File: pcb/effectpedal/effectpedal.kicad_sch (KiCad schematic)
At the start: 0 parts

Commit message: Made progress on the PCB
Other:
- company: (none) -> Anton Liakhovitch

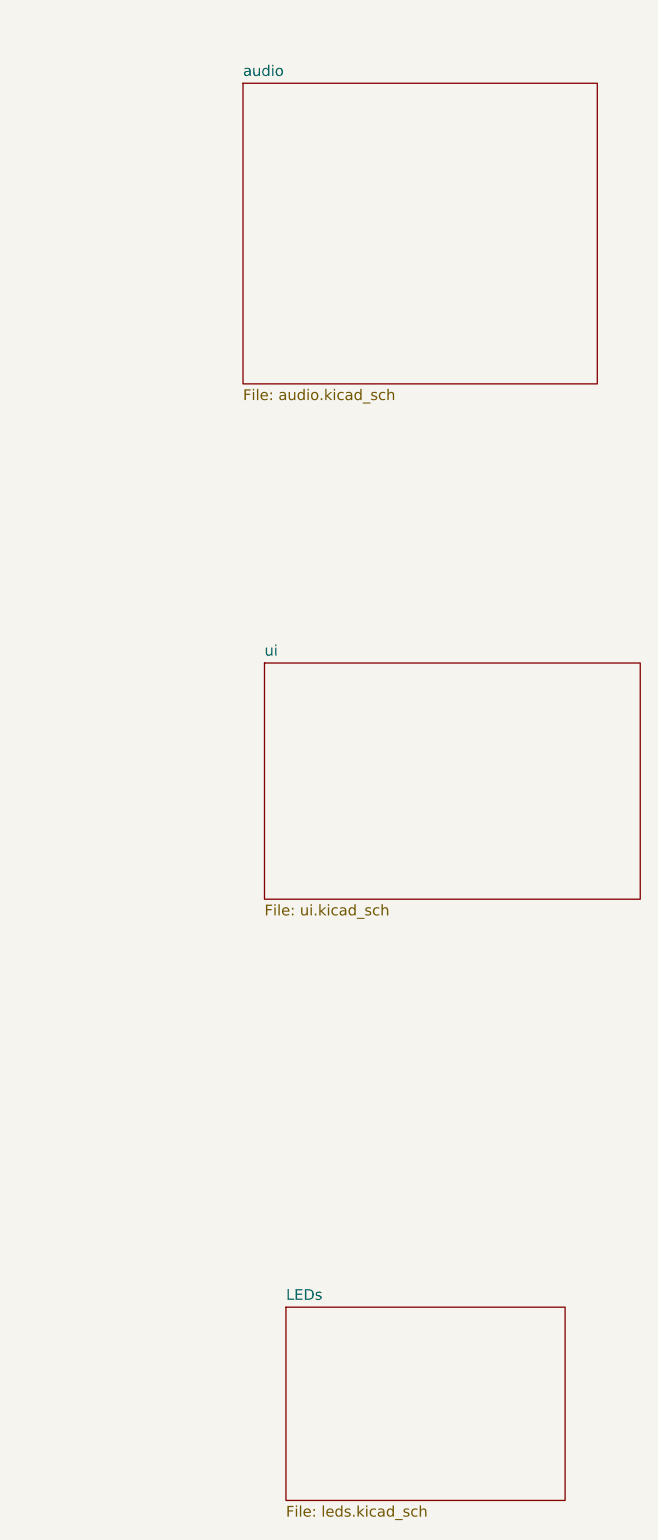
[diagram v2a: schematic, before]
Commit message: Added more test code and deleted some useless stuff
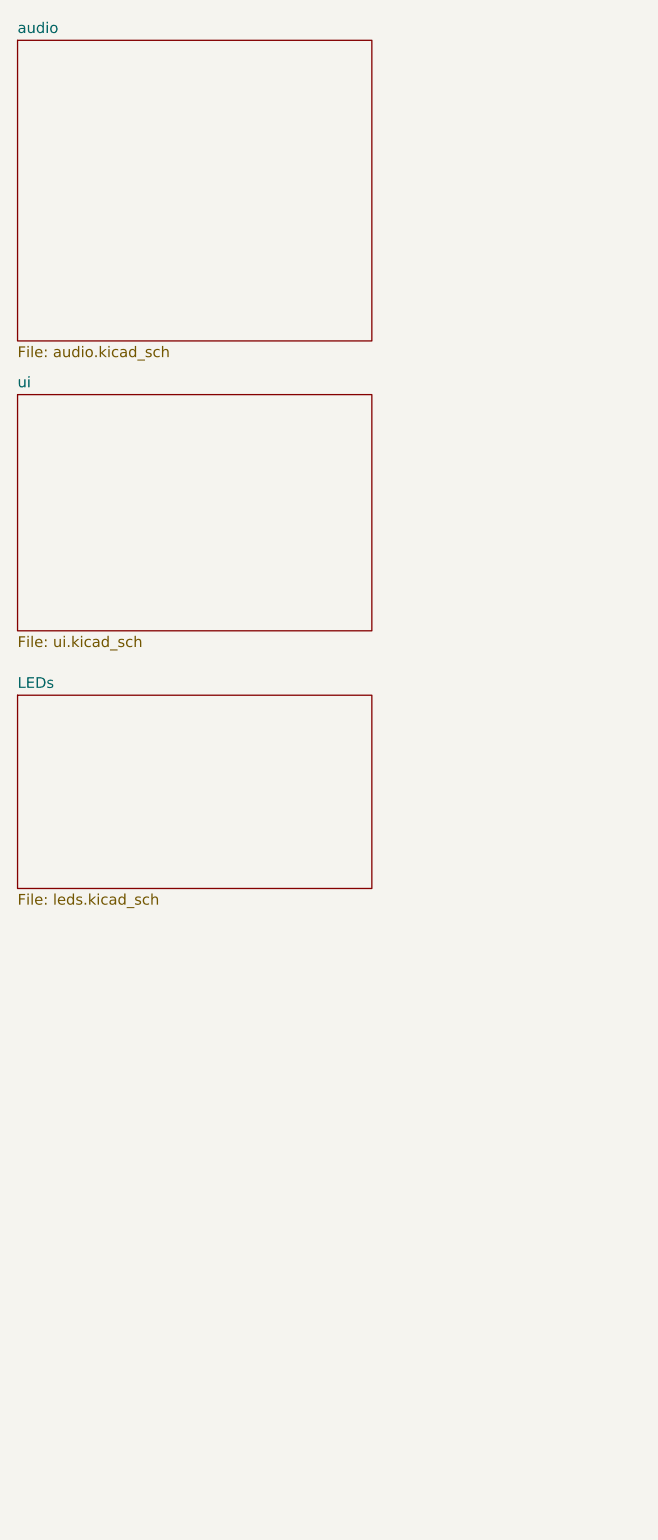
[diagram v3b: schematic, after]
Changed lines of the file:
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@@
     (company "Anton Liakhovitch")
   )
-  (sheet (at 43.18 90.17) (size 44.45 27.94) (fields_autoplaced)
+  (sheet (at 13.97 58.42) (size 41.91 27.94) (fields_autoplaced)
     (stroke (width 0.1524) (type solid) (color 0 0 0 0))
     (fill (color 0 0 0 0.0000))
-    (property "Sheet name" "ui" (id 0) (at 43.18 89.4584 0)
+    (property "Sheet name" "ui" (id 0) (at 13.97 57.7084 0)
       (effects (font (size 1.27 1.27)) (justify left bottom))
     )
-    (property "Sheet file" "ui.kicad_sch" (id 1) (at 43.18 118.6946 0)
+    (property "Sheet file" "ui.kicad_sch" (id 1) (at 13.97 86.9446 0)
       (effects (font (size 1.27 1.27)) (justify left top))
     )
   )
-  (sheet (at 40.64 21.59) (size 41.91 35.56) (fields_autoplaced)
+  (sheet (at 13.97 16.51) (size 41.91 35.56) (fields_autoplaced)
     (stroke (width 0.1524) (type solid) (color 0 0 0 0))
     (fill (color 0 0 0 0.0000))
-    (property "Sheet name" "audio" (id 0) (at 40.64 20.8784 0)
+    (property "Sheet name" "audio" (id 0) (at 13.97 15.7984 0)
       (effects (font (size 1.27 1.27)) (justify left bottom))
     )
-    (property "Sheet file" "audio.kicad_sch" (id 1) (at 40.64 57.7346 0)
+    (property "Sheet file" "audio.kicad_sch" (id 1) (at 13.97 52.6546 0)
       (effects (font (size 1.27 1.27)) (justify left top))
     )
   )
-  (sheet (at 45.72 166.37) (size 33.02 22.86) (fields_autoplaced)
+  (sheet (at 13.97 93.98) (size 41.91 22.86) (fields_autoplaced)
     (stroke (width 0.1524) (type solid) (color 0 0 0 0))
     (fill (color 0 0 0 0.0000))
-    (property "Sheet name" "LEDs" (id 0) (at 45.72 165.6584 0)
+    (property "Sheet name" "LEDs" (id 0) (at 13.97 93.2684 0)
       (effects (font (size 1.27 1.27)) (justify left bottom))
     )
-    (property "Sheet file" "leds.kicad_sch" (id 1) (at 45.72 189.8146 0)
+    (property "Sheet file" "leds.kicad_sch" (id 1) (at 13.97 117.4246 0)
       (effects (font (size 1.27 1.27)) (justify left top))
     )
